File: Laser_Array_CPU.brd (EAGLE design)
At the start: 110.2 x 204.9 mm, 55 parts, among them IC1 PIC24FJ64GA004, J3 22-23-2021, M1 MOTOR, U2 MAX6817, U3 LP2985-28DBVTE4, U5 LP2985A-33DBVTE4, X1 22-23-2031, X4 22-23-2041, X5 22-23-2041, X6 22-23-2031

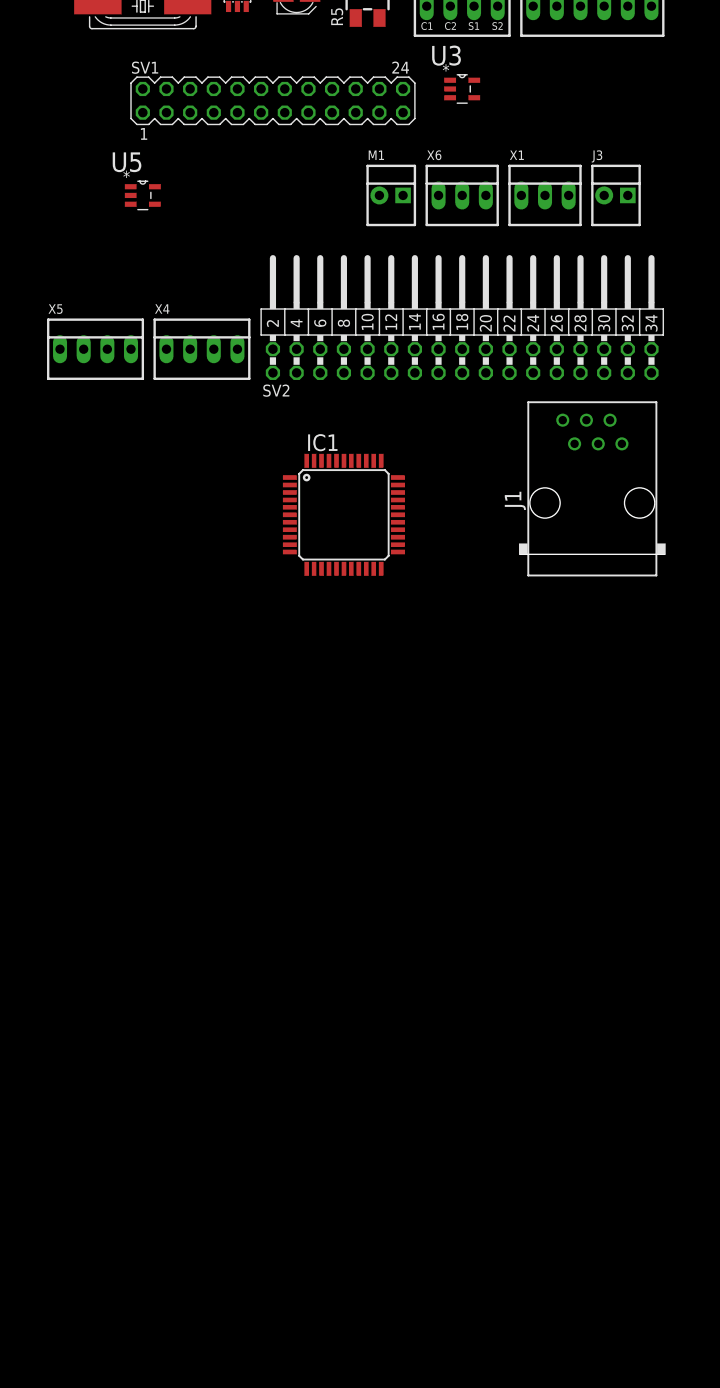
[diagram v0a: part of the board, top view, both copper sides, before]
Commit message: Started CPU Board
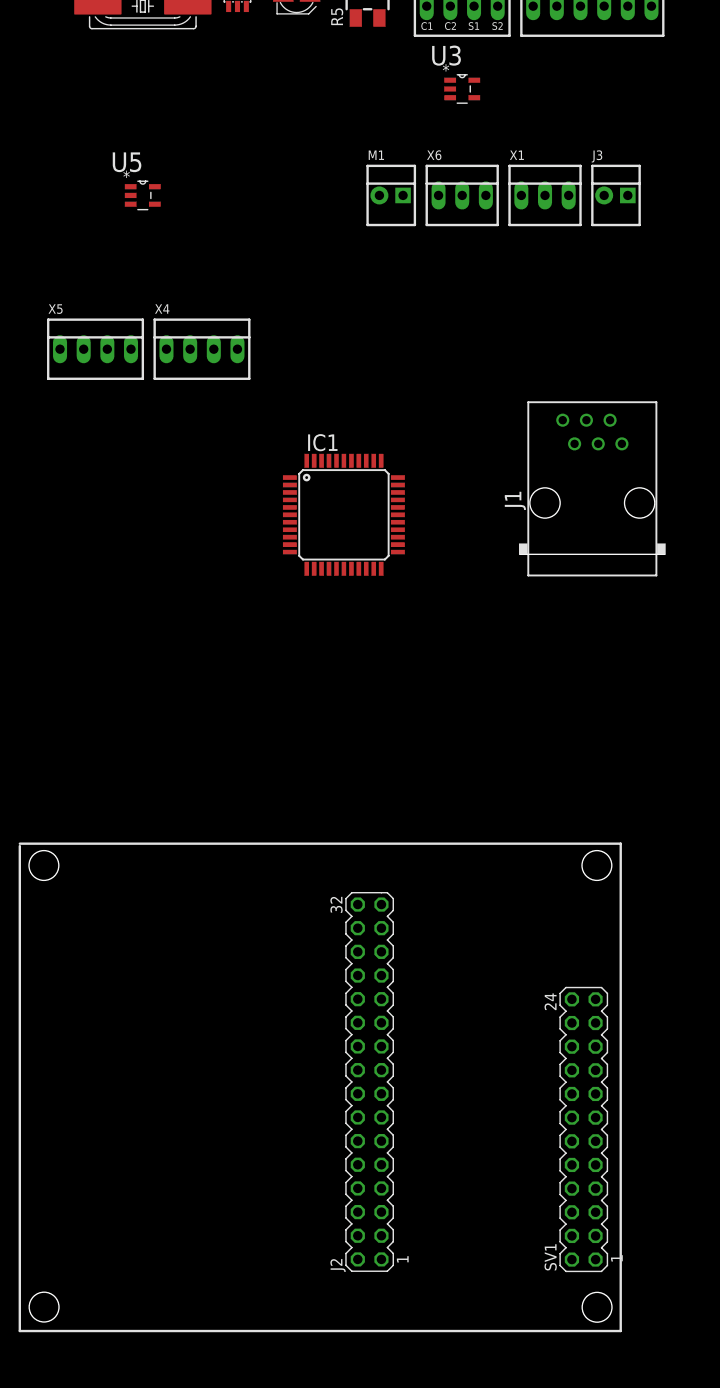
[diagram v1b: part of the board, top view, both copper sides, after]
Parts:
- removed SV2: (no value), con-lstb:MA17-2W
- added J2: MA16-2, Mine:MA16-2
- moved SV1 115.4 mm to (-22.5, -58.4), turned to 90 degrees
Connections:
- net GND: now also J2.25; no longer SV2.25
- net MOSI: now also J2.9; no longer SV2.9
- net SCLK: now also J2.11; no longer SV2.11
- net VDD: now also J2.29; no longer SV2.29

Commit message: temperture sensor board & CPU board complete
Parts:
- removed J2: MA16-2, Mine:MA16-2
- removed LED1, LED26: (no value), Mine:LED5MM
- removed M1: MOTOR, Mine:22-23-2021
- removed RLY1: RELAY_SPST, Mine:RELAY_SPST
- removed U5: LP2985A-33DBVTE4, Texas Instruments_By_element14_Batch_1:SOT95P280X145-5N
- removed X4: 22-23-2041, Mine:22-23-2041
- added C19: 470uF, rcl:PANASONIC_F
- added C20, C21: 10nF, rcl:C0805
- added D3, D4: 641-1014-6-ND, adafruit:SOD-123
- added D5: S10M-TPMSCT_ND, Mine:S10M-TPMSCT-ND
- added D7, D8: LL4148FSCT-ND, semicon-smd-ipc:SOD80
- added J4, J8, J9: 22-23-2021, Mine:22-23-2021
- added J6: (no value), Mine:RJ11-NO_SHIELD
- added Q5: (no value), Mine:SOT23-5L
- added R11: 200k, rcl:RTRIM3224X
- added R12: 10k, rcl:M0805
- added R15: 4.7k, rcl:M0805
- added R16: 10k, rcl:R0805
- added U1: MAX6817, Mine:SOT23-6
- added X2, X3: 22-23-2041, Mine:22-23-2041
- C10: value 10nF -> 0.1uF
- C11, C9: value 10nF -> 18pF
- C12: value 10nF -> 1uF
- C13, C18: value 2.2uF -> 10nF
- C16: value 1uF -> 2.2uF
- C17: value 0.1uF -> 2.2uF
- C2: value 0.1uF -> 10F; device rcl:C0805 -> rcl:E5-10,5
- C3: value 10uF -> 10F; device rcl:C0805 -> rcl:E5-10,5
- C4: value 18pF -> 0.1uF
- C5: value 18pF -> 10uF
- C7: value 10uF -> 0.1uF; device Mine:CAP3X3 -> rcl:C0805
- C8: value 0.1uF -> 10uF; device rcl:C0805 -> Mine:CAP3X3
- D1: value LL4148FSCT-ND -> S10M-TPMSCT_ND; device semicon-smd-ipc:SOD80 -> Mine:S10M-TPMSCT-ND
- D2: value LL4148FSCT-ND -> 641-1014-6-ND; device semicon-smd-ipc:SOD80 -> adafruit:SOD-123
- J1: value (none) -> MA16-2; device Mine:RJ11-NO_SHIELD -> Mine:MA16-2
- Q1: device adafruit:SM49 -> Mine:SOT23-5L
- Q4: device Mine:SOT23-5L -> adafruit:SM49
- R10: value 330 -> 220k; device rcl:R0805 -> rcl:M0805
- R13: value 4.7k -> 10k
- R14: value 4.7k -> 100k; device rcl:M0805 -> rcl:R0805
- R3: value 100k -> 10R, 5W; device rcl:R0805 -> Mine:RESISTOR5W
- R4: value 220k -> 100k; device rcl:M0805 -> rcl:R0805
- R5: value 200k -> 10k; device rcl:RTRIM3224X -> rcl:R0805
- R6, R7: value 10k -> 4.7k
- R8: value 10k -> 100k
- R9: value 100k -> 4.7k; device rcl:R0805 -> rcl:M0805
- S1: value TACT_PB -> (none); device Mine:PUSHBUTTON_SMD_SJ -> Mine:22-23-2061
- S2: value (none) -> TACT_PB; device Mine:22-23-2061 -> Mine:PUSHBUTTON_SMD_SJ
- U2: value MAX6817 -> LP2985-28DBVTE4; device Mine:SOT23-6 -> Texas Instruments_By_element14_Batch_1:SOT95P280X145-5N
- U3: value LP2985-28DBVTE4 -> LP2985A-33DBVTE4
- X6: value 22-23-2031 -> 22-23-2041; device Mine:22-23-2031 -> Mine:22-23-2041
- moved SV1 185.8 mm to (82.4, 94.9)
- moved S1 147.8 mm to (97.9, 80.9), turned to 90 degrees
- moved C3 146.7 mm to (64.1, 50.0), turned to 270 degrees
- moved J3 142.7 mm to (98.0, 123.6), turned to 90 degrees
- moved C13 141.2 mm to (68.7, 133.5)
- moved X1 139.8 mm to (98.0, 105.0), turned to 90 degrees
- moved R10 132.0 mm to (55.2, 138.9), turned to 180 degrees
- moved IC1 128.5 mm to (41.6, 99.5), turned to 180 degrees
- moved Q1 127.6 mm to (40.8, 125.9), turned to 270 degrees
- moved R8 123.4 mm to (48.3, 78.2), turned to 180 degrees
- moved J1 122.9 mm to (59.5, 101.3), turned to 90 degrees
- moved D2 122.5 mm to (40.1, 47.2), turned to 270 degrees
- moved U2 121.7 mm to (62.1, 134.3)
- moved R5 112.6 mm to (40.7, 135.6), turned to 90 degrees
- moved C1 109.3 mm to (67.4, 114.2), turned to 270 degrees
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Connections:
- removed net +12V_TB: M1.2, RLY1.1
- removed net A0: X5.3
- removed net ENSW: U2.1, X4.4
- removed net LASOUT: LED26.A, RLY1.4
- removed net N$12: M1.1, Q3.5
- removed net N$13: R5.3
- removed net N$14: U2.6
- removed net N$29: LED26.K, R10.2
- removed net N$3: J1.1
- removed net N$35 (its old number): C12.1, U5.4
- new net CHGOUTA: IC1.2, X1.1
- new net CHGOUTB: IC1.3, X1.2
- new net DISPWR: IC1.14, Q5.1, R14.1
- new net ENSW_I: R16.1, U1.1, X5.4
- new net ENSW_O: IC1.15, U1.6
- new net N$16: J4.1, Q2.5
- new net N$33: D3.C, D4.A, R3.2
- new net N$34: J8.1, Q3.5
- new net N$36: C2.-, C3.+
- new net N$37: C2.+, D5.A, R3.1
- new net N$55: C13.1, U2.4
- new net N$8: C1.2, J1.25, Q5.5
- new net VLASER: D1.C, X2.4, X6.4
- net !RESET: now also X6.3; no longer X5.4
- net +12V: now also C12.1, J3.1, R10.2, U2.1, U2.3, X2.2, X3.3; no longer C16.1, LED1.A, R4.2, U5.1, U5.3, X1.2, X6.2
- net CHGA: now also J9.1; no longer J3.1
- net CHGB: now also J9.2; no longer J3.2
- net ENCDR_A: now also C20.1, R12.1, X5.3; no longer C11.1, R7.1, X4.3
- net ENCDR_B: now also C18.1, R13.1, X5.2; no longer C10.1, R6.1, X4.2
- net EXFAN: now also Q2.1, R4.1; no longer Q3.1, R3.1
- net GND: now also C18.2, C19.-, C20.2, C21.2, C3.-, C7.1, C8.-, D8.2, J4.2, J6.4, J8.2, Q1.2, Q5.2, R11.1, R14.2, R4.2, R8.2, S1.4, S2.1, S2.2, U1.2, X1.3, X2.3, X3.4, X5.1; no longer C1.1, C2.2, C3.2, C7.-, C8.2, D2.2, J1.4, J2.25, Q4.2, R10.1, R3.2, R5.1, R9.2, S1.1, S1.2, S2.4, U5.2, X1.1, X4.1, X6.1
- net LASRLY: now also Q3.1, R8.1; no longer Q4.1, R9.1
- net MOSI: now also J1.9; no longer J2.9
- net N$1: now also C8.+, J6.6, R5.2, S2.3, S2.4; no longer C7.+, J1.6, R1.2, S1.3, S1.4
- net N$10: now also U1.4; no longer U2.4
- net N$11: now also J3.2, Q1.5; no longer LED1.K, Q2.5
- net N$15: now also D1.A, D2.C; no longer Q4.5, RLY1.2
- net N$2: now also C5.1; no longer C3.1
- net N$4: now also J6.2; no longer J1.2
- net N$5: now also J6.3; no longer J1.3
- net N$6: now also C9.1, Q4.1; no longer C5.1, Q1.1
- net N$7: now also C11.1, Q4.2; no longer C4.1, Q1.2
- net N$9: now also R1.1, S1.2, U1.3; no longer R8.1, S2.2, U2.3
- net ONLED: now also Q1.1; no longer Q2.1
- net SCL1: now also R7.1; no longer R14.1
- net SCL2: now also R15.1, X6.1; no longer X5.1
- net SCLK: now also J1.11; no longer J2.11
- net SDA1: now also R6.1; no longer R13.1
- net SDA2: now also R9.1, X6.2; no longer X5.2
- net VDD: now also C1.1, C10.1, C4.1, C7.2, D4.C, D5.C, J1.29, J6.5, R1.2, R12.2, R15.2, R16.2, R5.1, R9.2, U1.5, X3.1; no longer C1.2, C17.1, C2.1, C8.1, J1.5, J2.29, R1.1, R14.2, R8.2, S3.3, U2.5, X1.3, X6.3
- net VDD_TB: now also D2.A, D3.A, X2.1; no longer RLY1.3
- net VIN1: now also C21.1, D7.2, D8.1, R10.1, R11.2; no longer C9.1, D1.2, D2.1, R4.1, R5.2
- net VRR: now also C16.1, D7.1, U2.5; no longer C18.1, D1.1, U3.5
- net VTS: now also C17.1, C19.+, S3.3, U3.5, X3.2; no longer C13.1, U5.5
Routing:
- net +12V: track 0.00 -> 303.7 mm
- net VDD: track 0.00 -> 261.0 mm, vias 0 -> 10
- net N$34: track 0.00 -> 128.3 mm, vias 0 -> 2
- net CS: track 0.00 -> 120.1 mm
- net DC: track 0.00 -> 112.5 mm
- net CHGOUTA: track 0.00 -> 106.7 mm
- net CHGOUTB: track 0.00 -> 105.2 mm
- net SDA2: track 0.00 -> 97.2 mm, vias 0 -> 2
- net N$1: track 0.00 -> 93.7 mm, vias 0 -> 2
- net SCLK: track 0.00 -> 90.1 mm, vias 0 -> 4
- net MOSI: track 0.00 -> 87.5 mm, vias 0 -> 2
- net N$9: track 0.00 -> 86.7 mm, vias 0 -> 2
- net CHGA: track 0.00 -> 74.2 mm
- net CHGB: track 0.00 -> 73.6 mm
- net N$16: track 0.00 -> 70.9 mm, vias 0 -> 2
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- added copper zone on layer 1, net GND
- added copper zone on layer 16, net GND
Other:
- board size 110.2 x 204.9 mm -> 110.2 x 109.6 mm
- board text added: "August 23, 1018 Terawatt Productions Inc."
- board text added: "Laser_Array_CPU"
